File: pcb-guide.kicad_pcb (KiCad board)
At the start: 2 copper layers, 66.7 x 38.1 mm, 24 parts, among them SW1 SW_Push, U1 ATmega32U4-A, Y1 16MHz

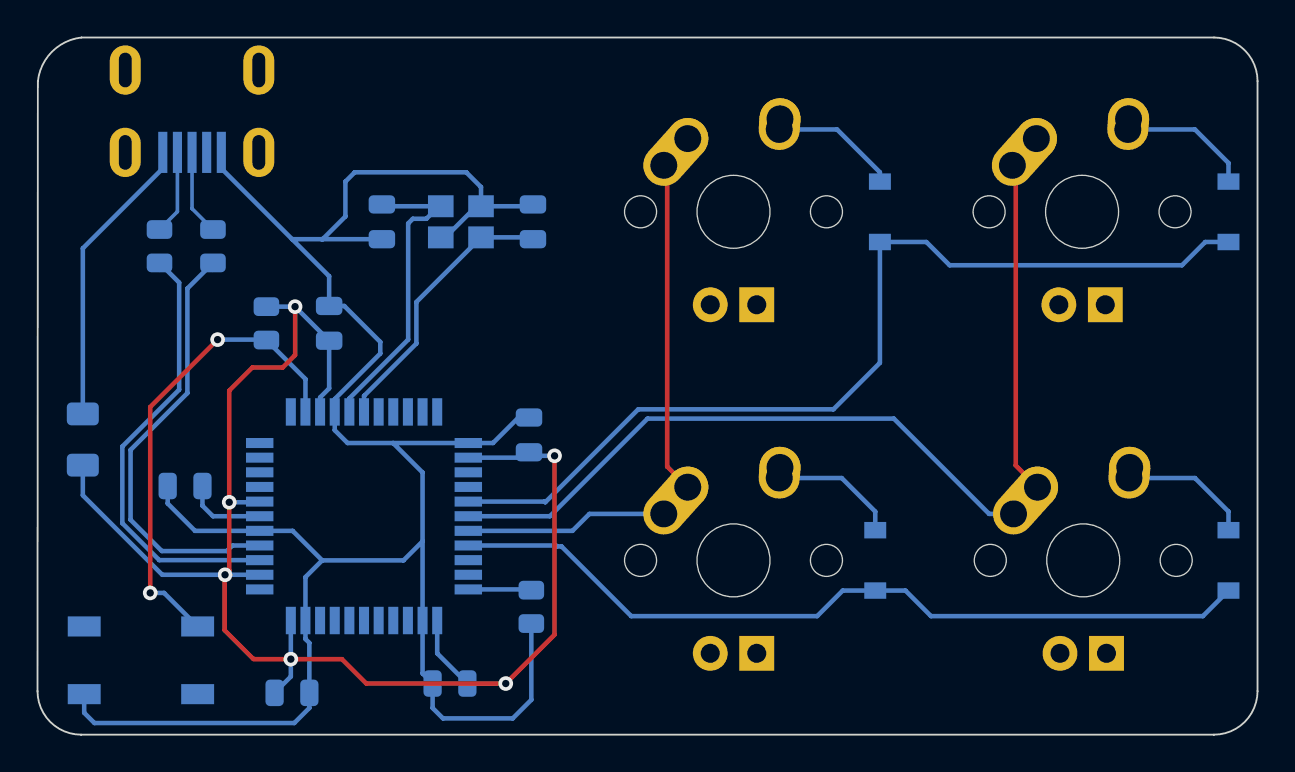
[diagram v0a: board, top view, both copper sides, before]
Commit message: Add submodules
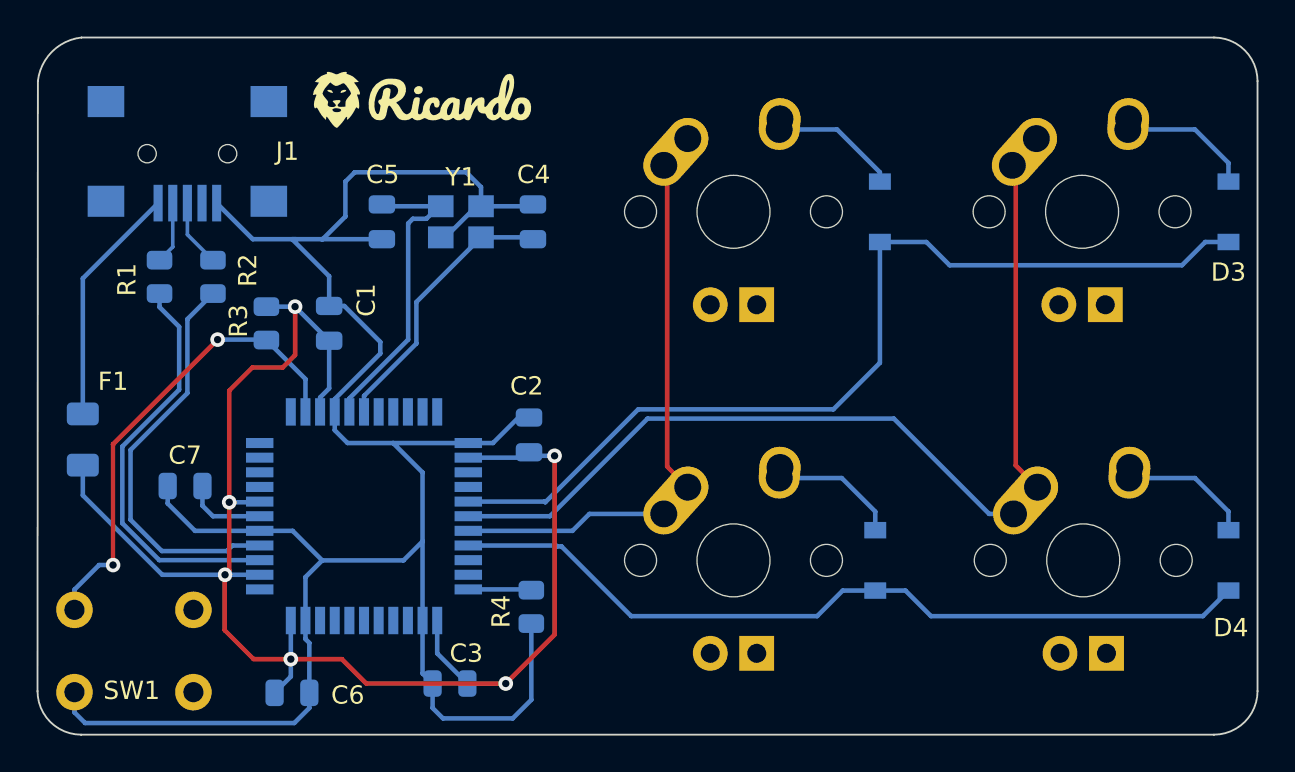
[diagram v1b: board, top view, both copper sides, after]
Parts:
- removed USB1: Molex-0548190589, random-keyboard-parts:Molex-0548190589
- added G***: LOGO, LOGO, F.Cu at (60.7, 82.8)
- added J1: USB_B_Mini, Connector_USB:USB_Mini-B_Lumberg_2486_01_Horizontal, B.Cu at (47.9, 85.7)
- SW1: footprint random-keyboard-parts:SKQG-1155865 -> Button_Switch_THT:SW_PUSH_6mm
- moved SW1 4.03 mm to (41.7, 115.2), turned to 0 degrees
- moved R1 1.67 mm to (46.4, 92.5)
- moved R2 1.67 mm to (49.3, 92.5)
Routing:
- net VCC: track 16.1 -> 13.2 mm
- net Net-(R2-Pad2): track 24.2 -> 22.1 mm
- net Net-(R1-Pad2): track 24.7 -> 22.6 mm
- net /D-: track 4.84 -> 3.42 mm
- net /D+: track 4.69 -> 3.70 mm
- net GND: track 119.8 -> 119.3 mm
